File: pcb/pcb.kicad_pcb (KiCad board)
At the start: 2 copper layers, 37 parts, among them J1 Conn_01x10, J2 Conn_01x05, J3 Conn_01x05, J4 Conn_01x05, J5 Conn_01x05, J6 Conn_01x05, J7 Conn_01x05, J8 Conn_01x05, U1 teensy-2.0

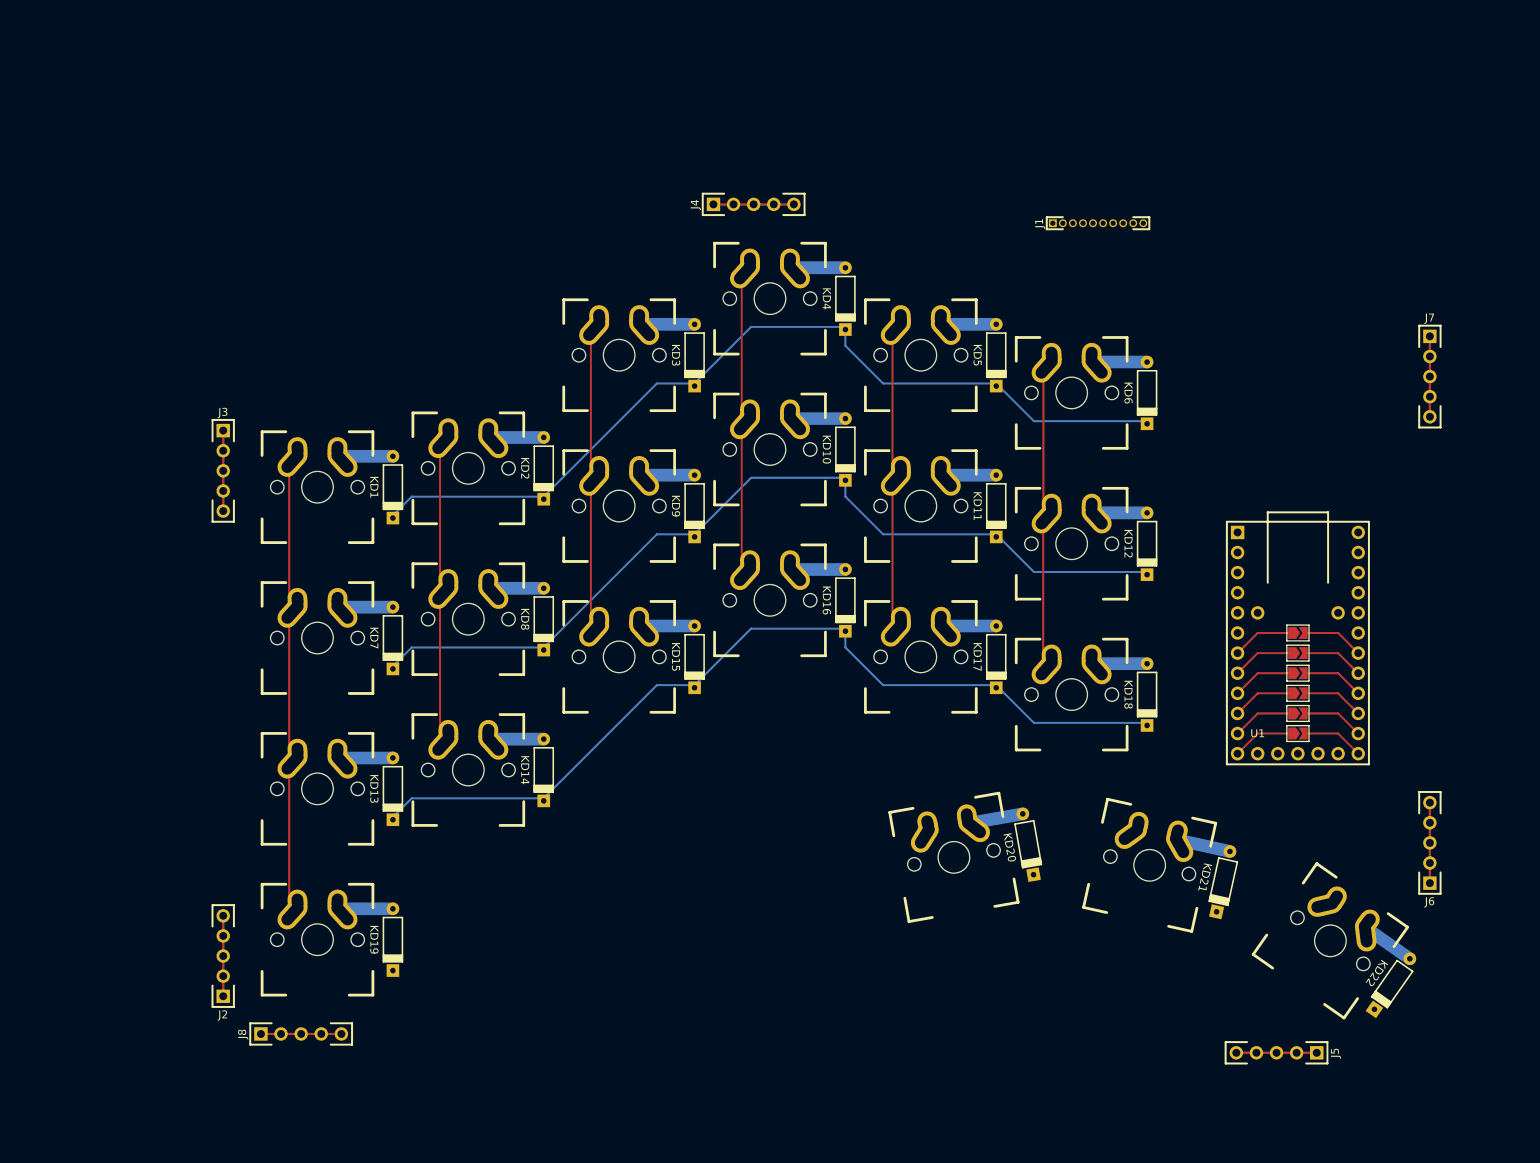
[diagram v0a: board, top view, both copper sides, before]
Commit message: Final routing of base pcb. Outline left.
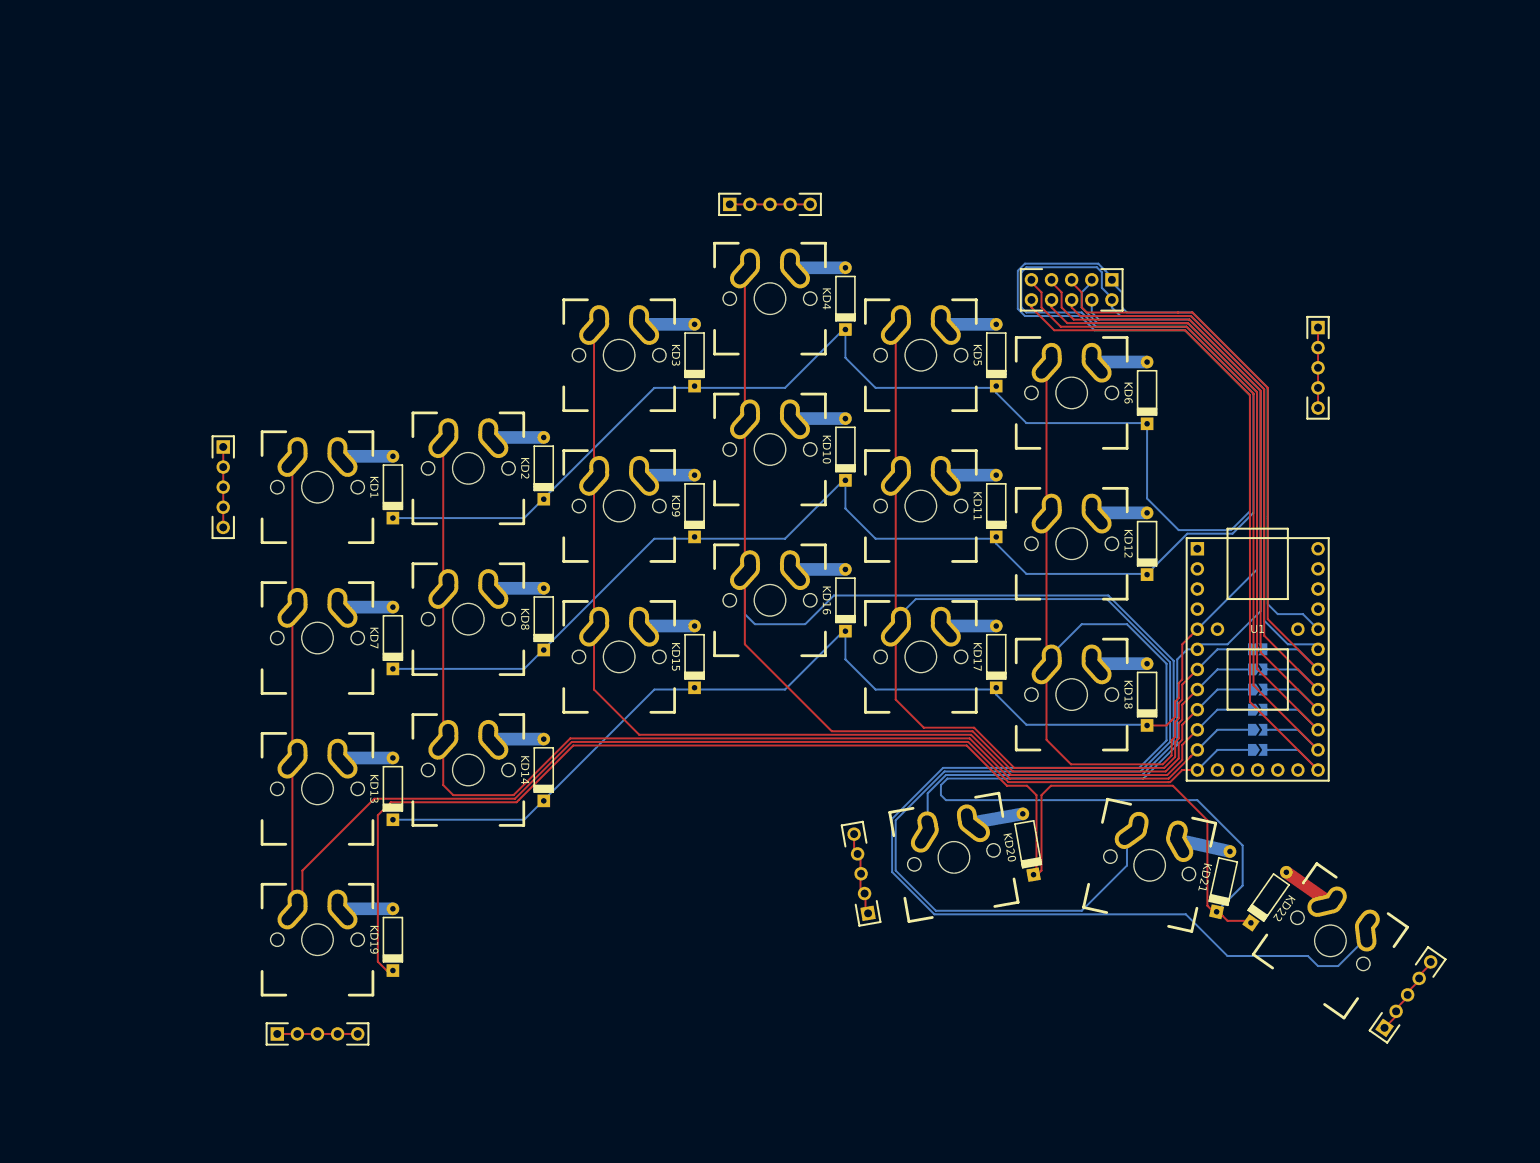
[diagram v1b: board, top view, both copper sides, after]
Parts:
- removed J8: Conn_01x05, keyboard-parts:header_1x05_2.54mm
- J1: footprint keyboard-parts:header_1x10_1.27mm -> keyboard-parts:header_2x05_2.54mm
- JP1, JP2, JP3, JP4, JP5, JP6, KD22: moved to B.Cu
- moved J2 118.7 mm to (-52.7, -71.4), turned to 90 degrees
- moved J4 118.4 mm to (-109.9, 33.3)
- moved J5 59.3 mm to (-35.2, 18.1), turned to 190 degrees
- moved J6 19.2 mm to (30.0, 32.6), turned to 145 degrees
- moved J7 14.2 mm to (21.6, -55.9)
- moved J1 10.3 mm to (-4.45, -61.9), turned to 270 degrees
- moved JP1 5.48 mm to (14.0, -2.54)
- moved JP2 5.48 mm to (14.0, -5.08)
- moved JP3 5.48 mm to (14.0, -7.62)
- moved JP4 5.48 mm to (14.0, -10.2)
- moved JP5 5.48 mm to (14.0, -12.7)
- moved JP6 5.48 mm to (14.0, -15.2)
- moved U1 5.48 mm to (14.0, -14.0)
- moved J3 2.06 mm to (-116.7, -40.8)
- turned KD22 to 145 degrees
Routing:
- net /R3: track 0.00 -> 332.4 mm
- net /C4-C7: track 47.8 -> 241.9 mm
- net /C3-C8: track 47.7 -> 236.0 mm
- net /C5-C6: track 50.8 -> 224.3 mm
- net /R0: track 112.1 -> 267.0 mm
- net /R1: track 112.1 -> 260.1 mm
- net /C0-CB: track 64.2 -> 191.3 mm
- net /C1-CA: track 47.7 -> 152.3 mm
- net /C2-C9: track 47.9 -> 136.3 mm
- net /Ext-C0-CB: track 7.78 -> 91.7 mm
- net /Ext-C1-CA: track 7.78 -> 91.3 mm
- net /R2: track 111.8 -> 192.8 mm
- net /Ext-C2-C9: track 7.78 -> 84.8 mm
- net /Ext-C3-C8: track 7.78 -> 84.4 mm
- net /Ext-C4-C7: track 7.78 -> 77.9 mm
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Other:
- board text added: "Grid for switch placement: 2.38125mm Grid for routing: 25 mils"
- board text added: "Right Side Jumpers"
- board text removed: "Grid for switch placement: 2.38125mm"

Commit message: Finish base pcb, decorations left
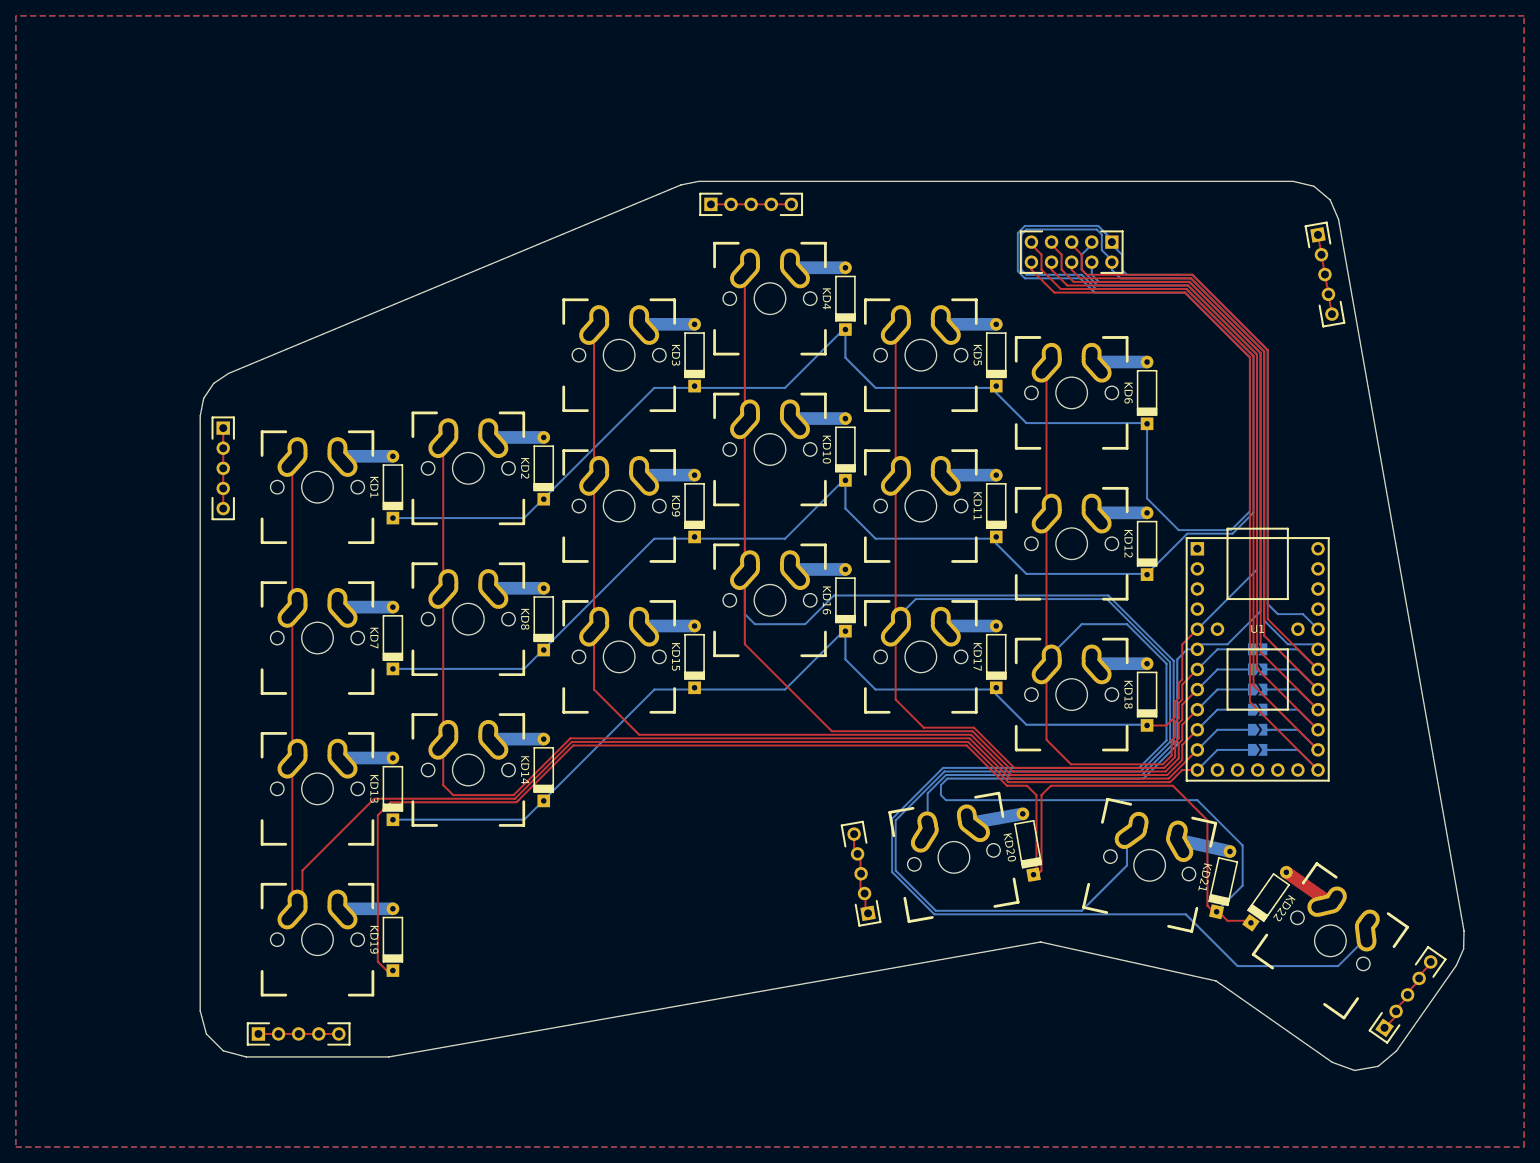
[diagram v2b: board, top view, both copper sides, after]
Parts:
- moved J7 11.7 mm to (21.6, -67.6), turned to 10 degrees
- moved J1 4.76 mm to (-4.45, -66.7)
- moved J2 2.38 mm to (-55.1, -71.4)
- moved J3 2.38 mm to (-116.7, -43.2)
- moved J4 2.38 mm to (-112.2, 33.3)
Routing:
- net /R0: track 267.0 -> 276.5 mm
- net /R1: track 260.1 -> 269.6 mm
- net /R2: track 192.8 -> 197.6 mm
- net /Ext-C1-CA: track 91.3 -> 96.1 mm
- net /Ext-C5-C6: track 77.5 -> 82.3 mm
- net /Ext-C3-C8: track 84.4 -> 89.2 mm
- net /Ext-C4-C7: track 77.9 -> 82.7 mm
- net /Ext-C2-C9: track 84.8 -> 89.6 mm
- net /Ext-C0-CB: track 91.7 -> 96.4 mm
- net /R3: track 332.4 -> 337.1 mm
- added copper zone on B.Cu, net (none)
- added copper zone on F.Cu, net (none)
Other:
- board outline added: 159.6 x 112.3 mm

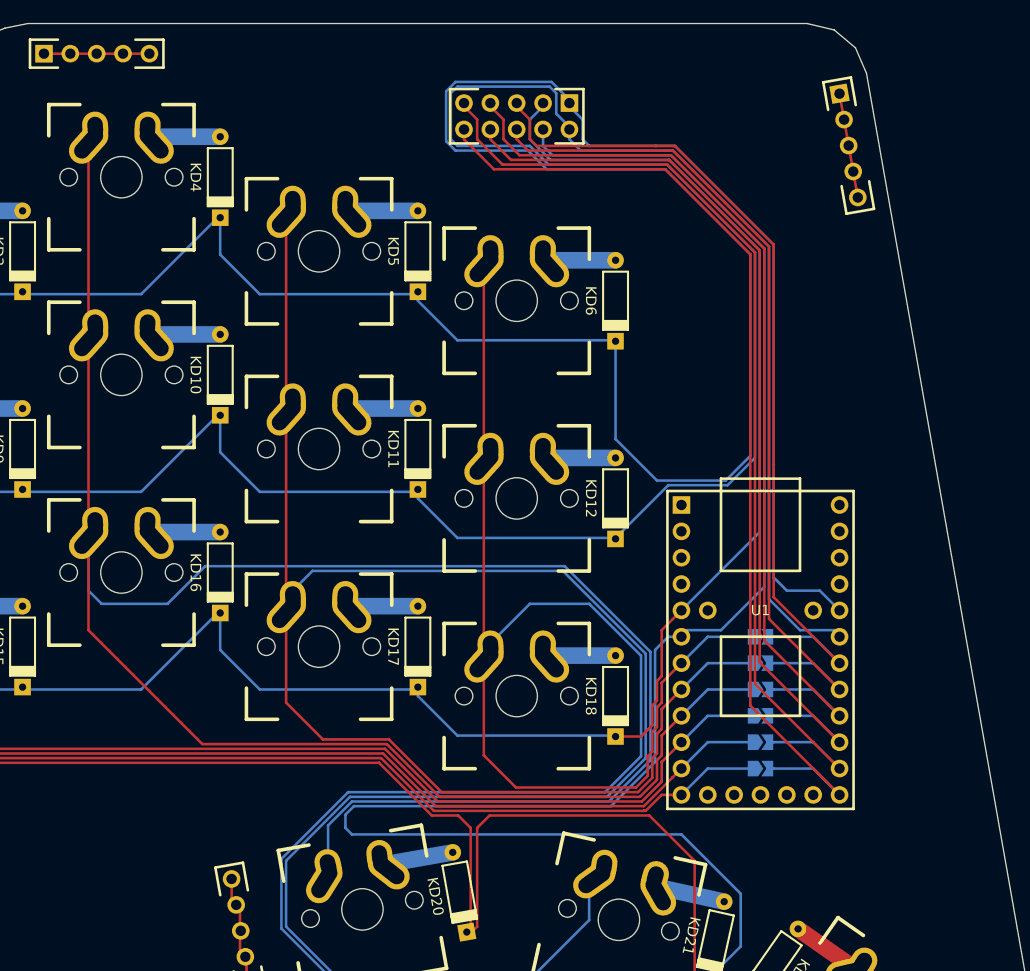
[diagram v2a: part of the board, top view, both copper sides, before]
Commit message: Add headers for board interconnect
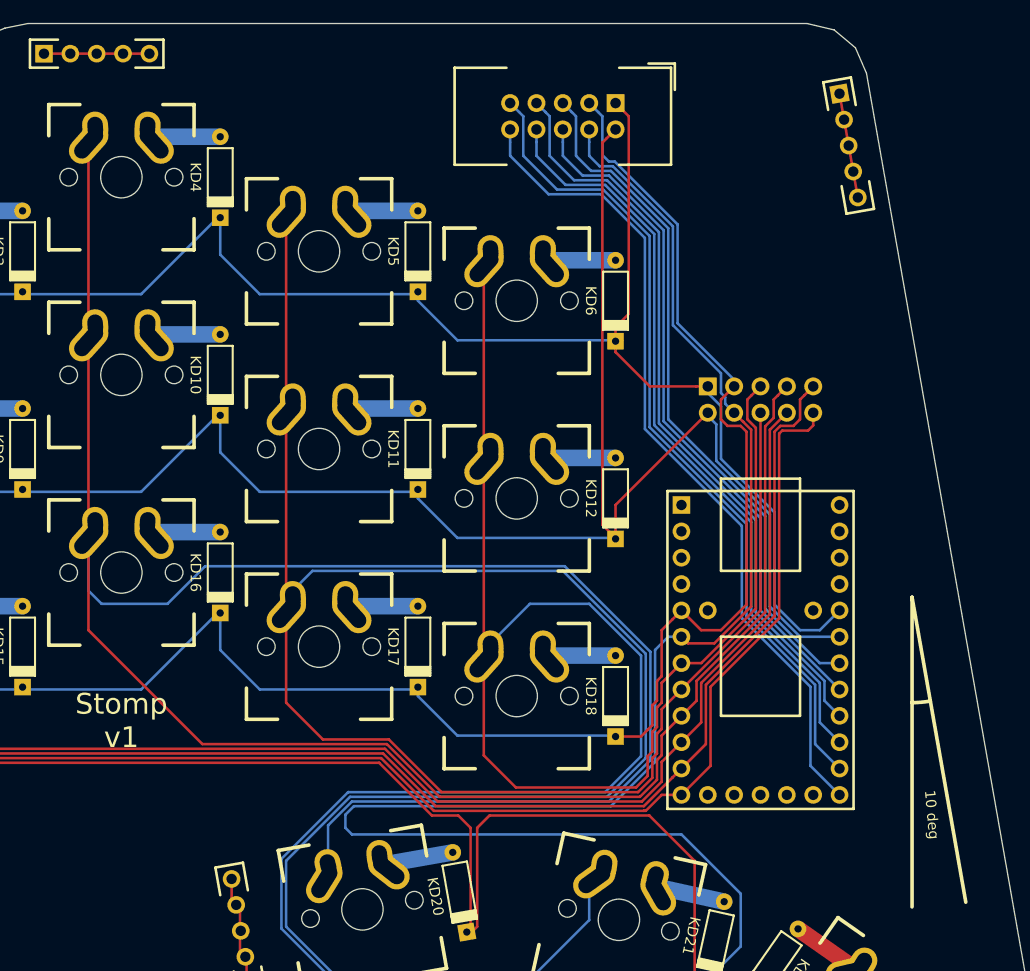
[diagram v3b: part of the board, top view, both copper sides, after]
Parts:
- removed JP1, JP2, JP3, JP4, JP5, JP6: SolderJumper_2_Open, keyboard-parts:solder-jumper-2p-open
- added J8: Conn_01x10, keyboard-parts:idc-header_2x05_2.54mm, B.Cu at (14.0, -39.4)
- J1: footprint keyboard-parts:header_2x05_2.54mm -> keyboard-parts:idc-header_2x05_2.54mm
- U1: footprint keyboard-parts:teensy2.0 -> keyboard-parts:teensy2.0_dualside
- moved J1 0.63 mm to (-5.08, -66.7), turned to 0 degrees
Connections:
- net /Ext-C0-CB renamed Net-(J1-Pad10)
- net /Ext-C1-CA renamed Net-(J1-Pad9)
- net /Ext-C2-C9 renamed Net-(J1-Pad8)
- net /Ext-C3-C8 renamed Net-(J1-Pad7)
- net /Ext-C4-C7 renamed Net-(J1-Pad6)
- net /Ext-C5-C6 renamed Net-(J1-Pad5)
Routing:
- net /R0: track 276.5 -> 180.8 mm
- net /R1: track 269.6 -> 198.6 mm
- net /C0-CB: track 191.3 -> 226.9 mm
- net /C1-CA: track 152.3 -> 187.2 mm
- net /C2-C9: track 136.3 -> 164.3 mm
- net /C3-C8: track 236.0 -> 264.0 mm
- net /C5-C6: track 224.2 -> 247.9 mm
- net /C4-C7: track 241.9 -> 263.8 mm
- net Net-(J1-Pad10): track 96.4 -> 80.3 mm
- net Net-(J1-Pad6): track 82.7 -> 66.5 mm
- net Net-(J1-Pad8): track 89.6 -> 73.4 mm
- net Net-(J1-Pad7): track 89.2 -> 73.0 mm
- net Net-(J1-Pad9): track 96.1 -> 79.9 mm
- net Net-(J1-Pad5): track 82.3 -> 67.3 mm
- net /R3: track 337.1 -> 329.3 mm
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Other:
- board text added: "10 deg"
- board text added: "M.Morin 2020"
- board text added: "Stomp v1"
- board text removed: "Right Side Jumpers"
